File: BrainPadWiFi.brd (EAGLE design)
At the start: 25.4 x 26 mm, 14 parts, among them IC1 ESP-WROOM-02FRONT-FACE, U1 LM3940IMP-3.3/NOPBMP04A-M

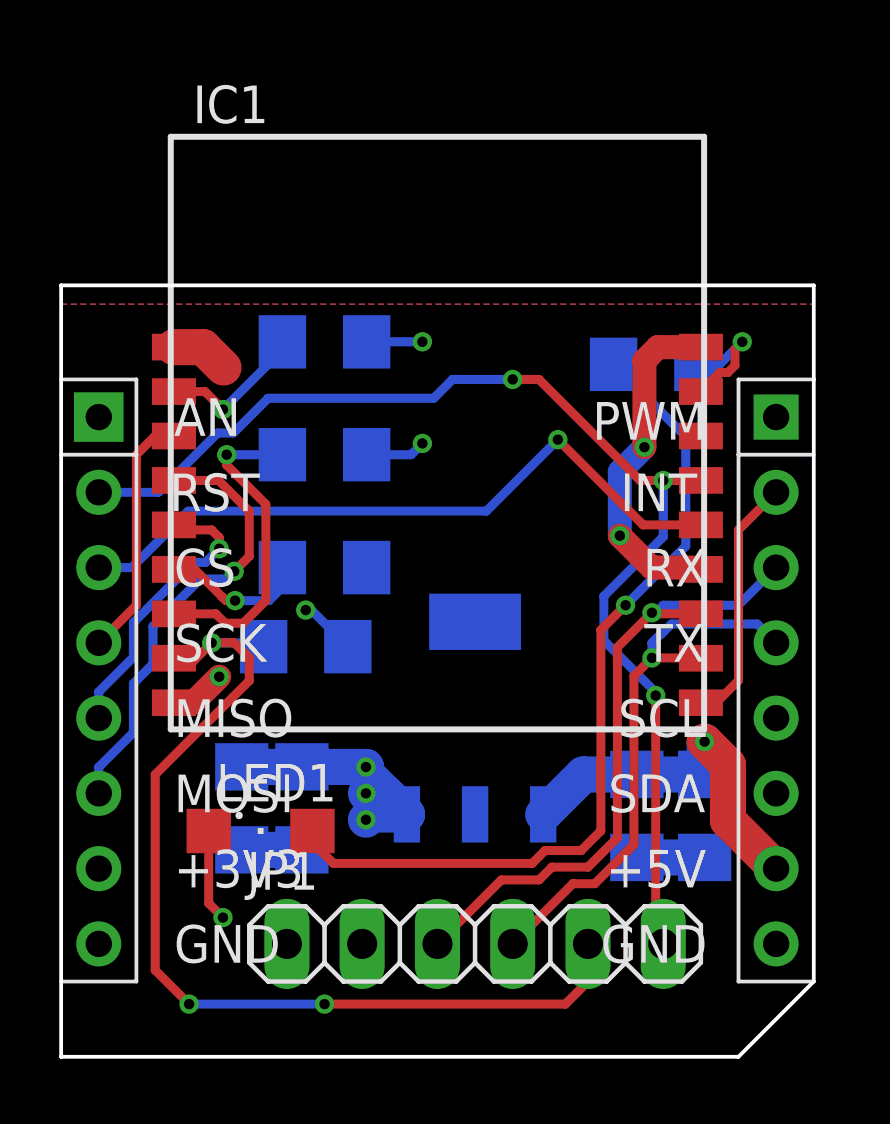
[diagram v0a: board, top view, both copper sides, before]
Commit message: Changed regulator.
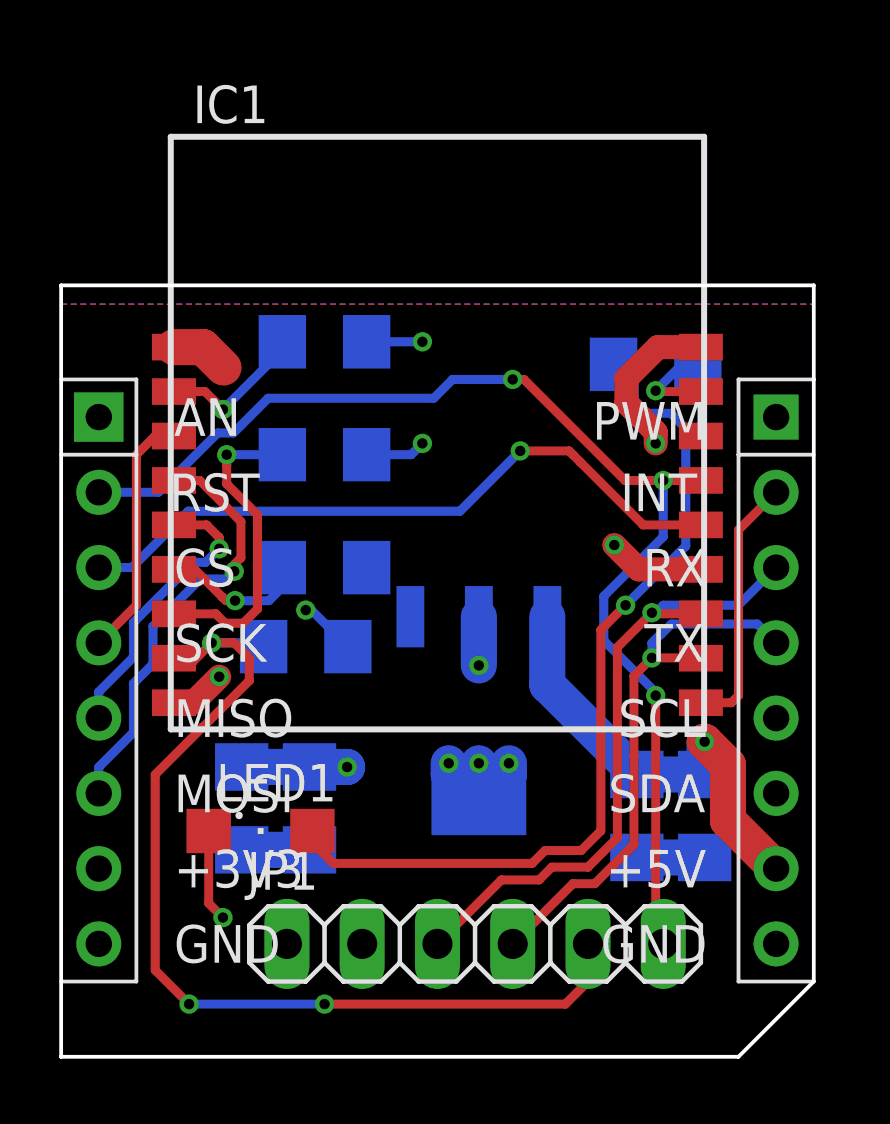
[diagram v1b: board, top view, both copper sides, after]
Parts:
- removed U1: LM3940IMP-3.3/NOPBMP04A-M, BrainPadWiFi:MP04A-M
- added U2: TLV1117LV33DCYRDCY4-M, BrainPadWiFi:DCY4-M
- moved C3 0.25 mm to (8.38, 8.38)
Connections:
- net 3V3: now also U2.2, U2.4; no longer U1.3
- net 5V: now also U2.3; no longer U1.1
- net GND: now also U2.1; no longer U1.2, U1.4
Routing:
- net 5V: track 12.4 -> 15.3 mm
- net GND: track 20.9 -> 18.4 mm
- net IO16: track 4.23 -> 3.33 mm
- net 3V3: track 17.3 -> 18.0 mm, vias 6 -> 8
- net MOSI: track 15.5 -> 14.9 mm
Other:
- board text added: "BrainPadWiFi 1.01"
- board text removed: "BrainPadWiFi 1.0"

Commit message: Panelized into 100x100mm for using Fusion PCB minimum PCB service.
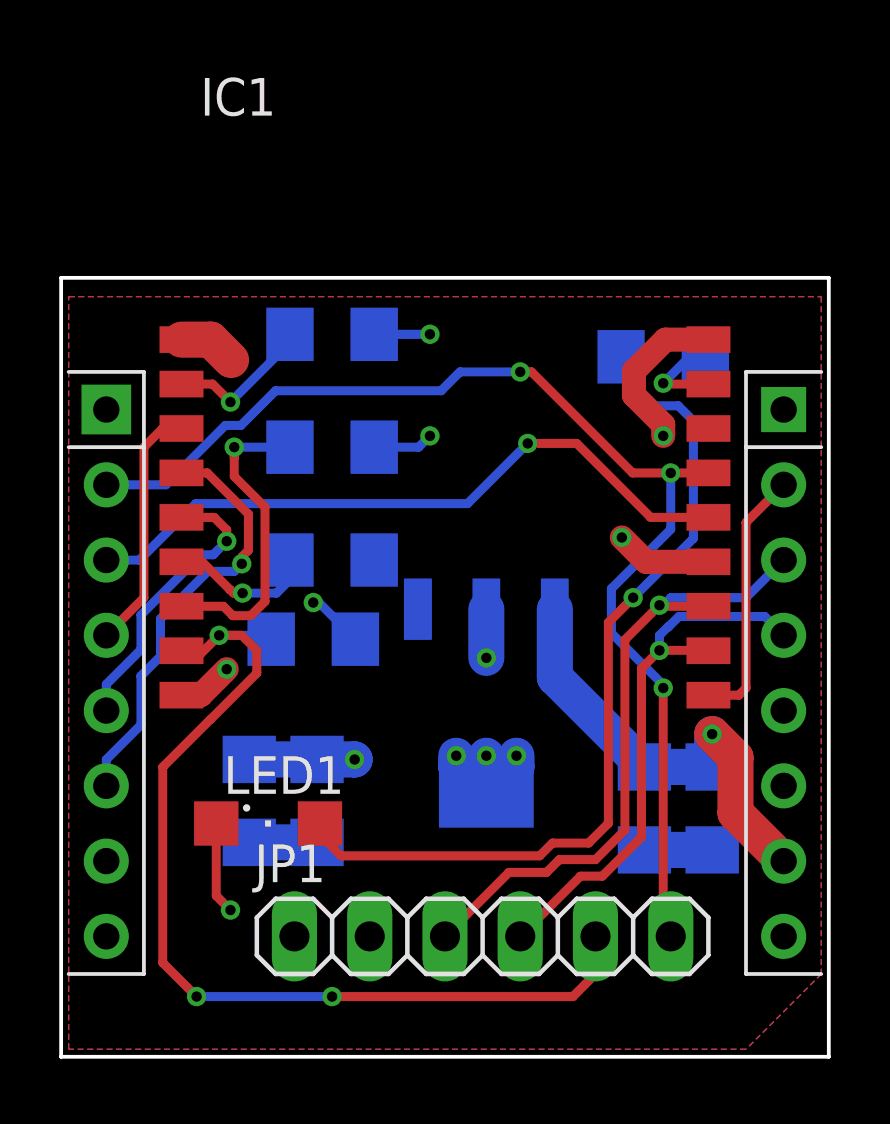
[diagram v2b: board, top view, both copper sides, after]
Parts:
- moved R4 0.36 mm to (20.3, 23.6)
- moved U2 0.36 mm to (14.4, 11.9)
- moved C4 0.36 mm to (22.0, 8.38)
- moved R1 0.36 mm to (9.14, 24.4)
- moved R2 0.36 mm to (9.14, 20.6)
- moved LED1 0.36 mm to (6.99, 7.87)
- moved U$1 0.36 mm to (0.25, 0.25)
- moved JP1 0.36 mm to (14.2, 4.06)
- moved C2 0.36 mm to (6.35, 8.64)
- moved C3 0.36 mm to (8.64, 8.64)
- moved IC1 0.36 mm to (13.0, 19.3)
- moved R3 0.36 mm to (8.51, 14.1)
- moved C1 0.36 mm to (19.7, 8.38)
- moved R5 0.36 mm to (9.14, 16.8)
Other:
- board size 25.4 x 26 mm -> 25.9 x 26.3 mm

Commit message: PROG line wired because we grant to an ability for self-programming from BrainPad to ESP.
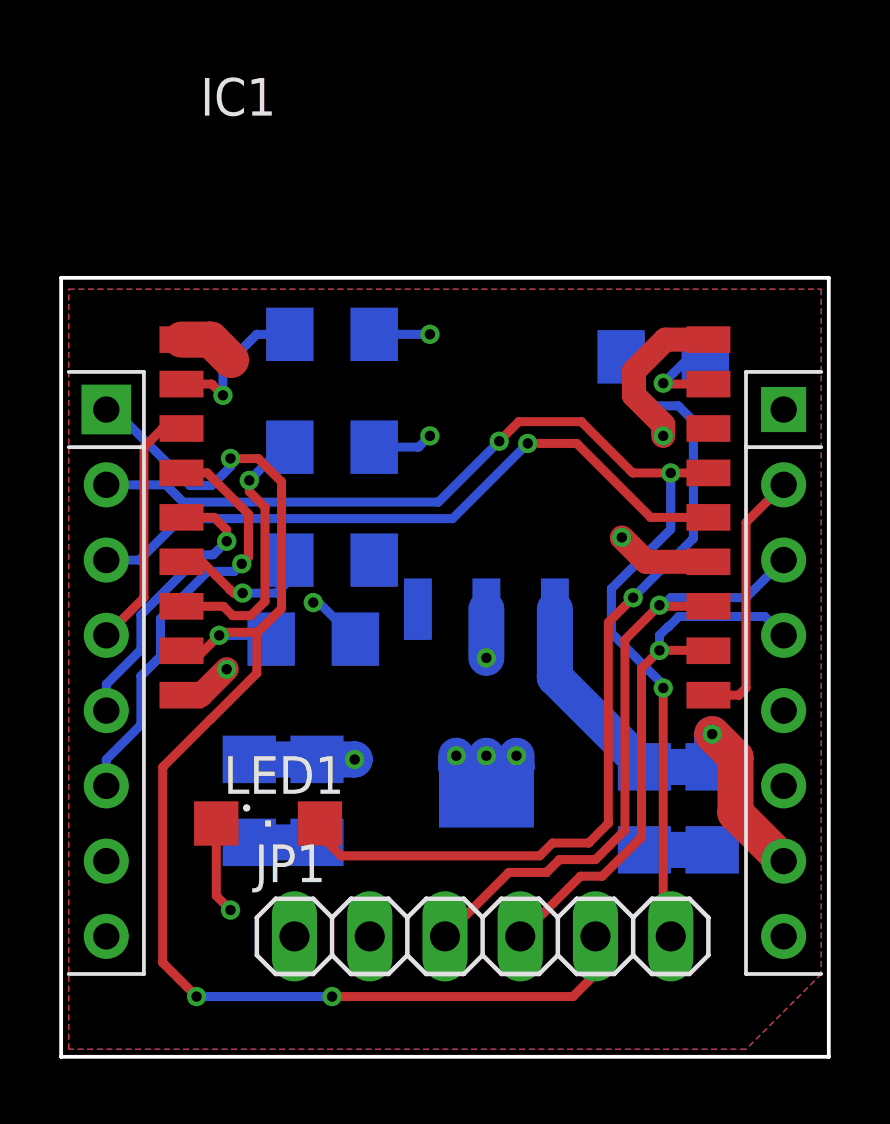
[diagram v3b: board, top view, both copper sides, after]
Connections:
- net PROG: now also U$1.P$1
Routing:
- net PROG: track 33.6 -> 47.4 mm, vias 3 -> 4
- net N$1: track 11.0 -> 9.29 mm
- net RST: track 40.6 -> 39.7 mm

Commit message: Redesigned for next version.
SMT pieces place only front side. (exclude ESP)
Add grove connector.
Registers only 1K.
Add status2 LED.
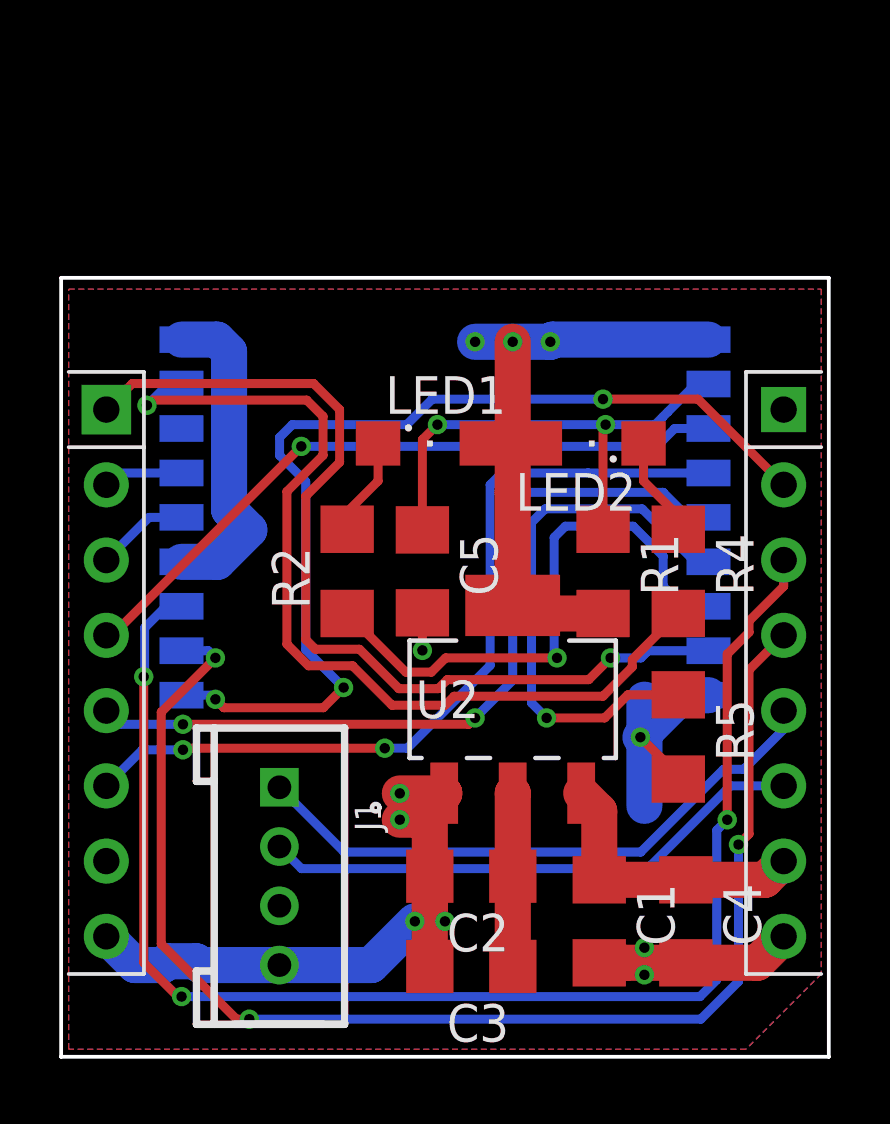
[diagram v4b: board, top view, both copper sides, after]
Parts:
- removed JP1: JP1, BrainPadWiFi:1X06
- removed R3: 10K, BrainPadWiFi:R1206
- added C5: 0.1u, BrainPadWiFi:C1206
- added J1: GROVE I2C, BrainPadWiFi:HW4-2.0
- added LED2: STATUS2, BrainPadWiFi:SML1206
- LED1: value STATUS -> STATUS1
- R1, R2, R5: value 10K -> 1K
- R4: value 470 -> 1K
- moved LED1 13.9 mm to (12.4, 20.7)
- moved R5 13.1 mm to (20.8, 10.8), flipped to the top, turned to 270 degrees
- moved R1 12.2 mm to (18.3, 16.4), flipped to the top, turned to 270 degrees
- moved C2 7.91 mm to (13.8, 6.10), flipped to the top, turned to 180 degrees
- moved C3 7.64 mm to (13.8, 3.05), flipped to the top, turned to 180 degrees
- moved R4 7.26 mm to (20.8, 16.4), flipped to the top, turned to 270 degrees
- moved R2 4.22 mm to (9.65, 16.4), flipped to the top, turned to 90 degrees
- moved C1 4.10 mm to (18.2, 4.57), flipped to the top
- moved C4 3.91 mm to (21.1, 4.57), flipped to the top
- moved U2 0.90 mm to (15.2, 12.1), flipped to the top, turned to 0 degrees
- flipped IC1 to the bottom
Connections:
- net N$1 renamed IO2
- net N$4 renamed IO15
- removed net STAT: LED1.A, R4.1
- new net SCL: J1.1, U$1.P$12
- new net SDA: J1.2, U$1.P$11
- new net STAT1: LED1.C, R2.2
- new net STAT2: LED2.C, R4.1
- net 3V3: now also J1.3, LED1.A, LED2.A; no longer JP1.1, R2.2, R3.2
- net EN: now also C5.1
- net GND: now also C5.2, J1.4; no longer JP1.2, LED1.C
- net PROG: no longer JP1.5, R3.1
- net RST: no longer JP1.6
- net RX: no longer JP1.3
- net TX: no longer JP1.4
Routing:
- net RST: track 39.7 -> 2.70 mm, vias 3 -> 0
- net GND: track 18.4 -> 51.2 mm, vias 4 -> 8
- net STAT: track 29.3 -> 0.00 mm, vias 1 -> 0
- net IO16: track 3.33 -> 31.5 mm
- net TX: track 18.9 -> 45.0 mm, vias 1 -> 3
- net RX: track 22.1 -> 48.0 mm, vias 1 -> 3
- net INT: track 8.75 -> 34.0 mm, vias 0 -> 3
- net SCL: track 0.00 -> 20.3 mm
- net CS: track 23.0 -> 3.13 mm, vias 1 -> 0
- net SDA: track 0.00 -> 18.5 mm
- net MISO: track 9.72 -> 27.6 mm, vias 1 -> 2
- net PROG: track 47.4 -> 31.6 mm, vias 4 -> 1
- net SCK: track 8.40 -> 23.2 mm, vias 0 -> 1
- net IO15: track 5.03 -> 18.5 mm
- net MOSI: track 14.9 -> 28.3 mm, vias 1 -> 2
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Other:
- board text added: "BrainPadWiFi 1.1"
- board text added: "STAT1"
- board text removed: "3.3V"
- board text removed: "BrainPadWiFi 1.01"
- board text removed: "GND"
- board text removed: "PG"
- board text removed: "RST"
- board text removed: "RXD"
- board text removed: "STAT"
- board text removed: "TXD"

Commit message: Add grove icon.
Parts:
- added U$2: (no value), BrainPadWiFi:TWIGLOGO_SMALL
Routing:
- net 3V3: track 27.8 -> 40.6 mm
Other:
- board text added: "S1 S2"
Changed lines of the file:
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@@
 <wire x1="22.733" y1="1.016" x2="1.016" y2="1.016" width="1.2192" layer="48"/>
 <wire x1="1.016" y1="1.016" x2="1.016" y2="25.273" width="1.2192" layer="48"/>
+<text x="13.462" y="18.542" size="0.8128" layer="48" font="vector" ratio="15">S1  S2</text>
 </plain>
 <attributes>
@@
 <element name="LED1" library="BrainPadWiFi" package="SML1206" package3d_urn="urn:adsk.eagle:package:15829/1" value="STATUS1" x="12.446" y="20.701"/>
 <element name="J1" library="BrainPadWiFi" package="HW4-2.0" value="GROVE I2C" x="7.366" y="6.096" rot="R270"/>
+<element name="U$2" library="BrainPadWiFi" package="TWIGLOGO_SMALL" value="" x="3.175" y="14.224"/>
 </elements>
 <signals>
@@
 <wire x1="15.24" y1="19.05" x2="15.24" y2="20.701" width="1.2192" layer="1"/>
 <wire x1="15.24" y1="20.701" x2="15.24" y2="24.13" width="1.2192" layer="1"/>
+<wire x1="15.243" y1="3.048" x2="15.243" y2="1.273" width="1.2192" layer="1"/>
+<wire x1="15.243" y1="1.273" x2="15.24" y2="1.27" width="1.2192" layer="1"/>
+<wire x1="15.24" y1="1.27" x2="15.2256" y2="1.2844" width="1.2192" layer="1"/>
+<wire x1="10.747" y1="4.493" x2="10.16" y2="5.08" width="1.2192" layer="1"/>
+<wire x1="15.2256" y1="1.2844" x2="11.2852875" y2="1.2844" width="1.2192" layer="1"/>
+<wire x1="11.2852875" y1="1.2844" x2="10.747" y2="1.8226875" width="1.2192" layer="1"/>
+<wire x1="10.747" y1="1.8226875" x2="10.747" y2="4.493" width="1.2192" layer="1"/>
+<wire x1="10.16" y1="5.08" x2="7.382" y2="5.08" width="1.2192" layer="1"/>
+<wire x1="7.382" y1="5.08" x2="7.366" y2="5.096" width="1.2192" layer="1"/>
 </signal>
 <signal name="RX">
@@
 <wire x1="17.78" y1="19.704" x2="14.878" y2="19.704" width="0.3048" layer="16"/>
 <wire x1="14.878" y1="19.704" x2="14.478" y2="19.304" width="0.3048" layer="16"/>
-<wire x1="14.478" y1="19.304" x2="14.478" y2="13.208" width="0.3048" layer="16"/>
-<wire x1="11.684" y1="10.414" x2="10.922" y2="10.414" width="0.3048" layer="16"/>
-<via x="10.922" y="10.414" extent="1-16" drill="0.35"/>
-<wire x1="10.922" y1="10.414" x2="4.1632" y2="10.414" width="0.3048" layer="1"/>
-<wire x1="4.1632" y1="10.414" x2="4.111" y2="10.3618" width="0.3048" layer="1"/>
-<wire x1="14.478" y1="13.208" x2="11.684" y2="10.414" width="0.3048" layer="16"/>
+<wire x1="4.237" y1="10.4878" x2="4.111" y2="10.3618" width="0.3048" layer="1"/>
+<wire x1="12.5198" y1="10.4878" x2="12.446" y2="10.4878" width="0.3048" layer="16"/>
+<via x="12.446" y="10.4878" extent="1-16" drill="0.35"/>
+<wire x1="14.478" y1="19.304" x2="14.478" y2="12.446" width="0.3048" layer="16"/>
+<wire x1="14.478" y1="12.446" x2="12.5198" y2="10.4878" width="0.3048" layer="16"/>
+<wire x1="12.446" y1="10.4878" x2="4.237" y2="10.4878" width="0.3048" layer="1"/>
 </signal>
 <signal name="MISO">
@@
 <wire x1="20.32" y1="19.05" x2="21.166" y2="18.204" width="0.3048" layer="16"/>
 <wire x1="20.32" y1="19.05" x2="15.621" y2="19.05" width="0.3048" layer="16"/>
-<via x="13.97" y="11.4356" extent="1-16" drill="0.35"/>
-<wire x1="13.756" y1="11.2216" x2="13.97" y2="11.4356" width="0.3048" layer="1"/>
-<wire x1="4.111" y1="11.2216" x2="13.756" y2="11.2216" width="0.3048" layer="1"/>
-<wire x1="15.621" y1="19.05" x2="15.24" y2="18.669" width="0.3048" layer="16"/>
-<wire x1="15.24" y1="18.669" x2="15.24" y2="12.7056" width="0.3048" layer="16"/>
-<wire x1="15.24" y1="12.7056" x2="13.97" y2="11.4356" width="0.3048" layer="16"/>
+<wire x1="15.24" y1="18.669" x2="15.621" y2="19.05" width="0.3048" layer="16"/>
+<wire x1="14.391" y1="11.2216" x2="14.605" y2="11.4356" width="0.3048" layer="1"/>
+<via x="14.605" y="11.4356" extent="1-16" drill="0.35"/>
+<wire x1="14.605" y1="11.4356" x2="15.24" y2="12.0706" width="0.3048" layer="16"/>
+<wire x1="4.111" y1="11.2216" x2="14.391" y2="11.2216" width="0.3048" layer="1"/>
+<wire x1="15.24" y1="12.0706" x2="15.24" y2="18.669" width="0.3048" layer="16"/>
 </signal>
 <signal name="RST">
@@
 <wire x1="11.66225" y1="21.33521875" x2="7.80145" y2="21.33521875" width="0.3048" layer="16"/>
 <wire x1="12.52205" y1="22.19501875" x2="11.66225" y2="21.33521875" width="0.3048" layer="16"/>
-<wire x1="8.255" y1="13.7397125" x2="9.5327125" y2="12.462" width="0.3048" layer="16"/>
 <via x="9.5327125" y="12.462" extent="1-16" drill="0.35"/>
 <via x="5.207" y="12.065" extent="1-16" drill="0.35"/>
 <wire x1="5.207" y1="12.065" x2="5.068" y2="12.204" width="0.3048" layer="16"/>
 <wire x1="5.068" y1="12.204" x2="4.0615" y2="12.204" width="0.3048" layer="16"/>
-<wire x1="8.255" y1="19.41406875" x2="8.255" y2="13.7397125" width="0.3048" layer="16"/>
+<wire x1="8.255" y1="19.41406875" x2="8.255" y2="13.97" width="0.3048" layer="16"/>
 <wire x1="9.5327125" y1="12.462" x2="8.8511125" y2="11.7804" width="0.3048" layer="1"/>
 <wire x1="5.4916" y1="11.7804" x2="5.207" y2="12.065" width="0.3048" layer="1"/>
 <wire x1="8.8511125" y1="11.7804" x2="5.4916" y2="11.7804" width="0.3048" layer="1"/>
+<wire x1="8.255" y1="13.97" x2="8.763" y2="13.462" width="0.3048" layer="16"/>
+<wire x1="9.144" y1="13.462" x2="9.525" y2="13.081" width="0.3048" layer="16"/>
+<wire x1="9.525" y1="13.081" x2="9.525" y2="12.4697125" width="0.3048" layer="16"/>
+<wire x1="9.525" y1="12.4697125" x2="9.5327125" y2="12.462" width="0.3048" layer="16"/>
+<wire x1="8.763" y1="13.462" x2="9.144" y2="13.462" width="0.3048" layer="16"/>
 </signal>
 <signal name="PROG">
